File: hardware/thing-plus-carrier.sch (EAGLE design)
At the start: 6 parts, among them J1 THING_PLUS, U1 OKI-78SR-5/1.5-W36H-C

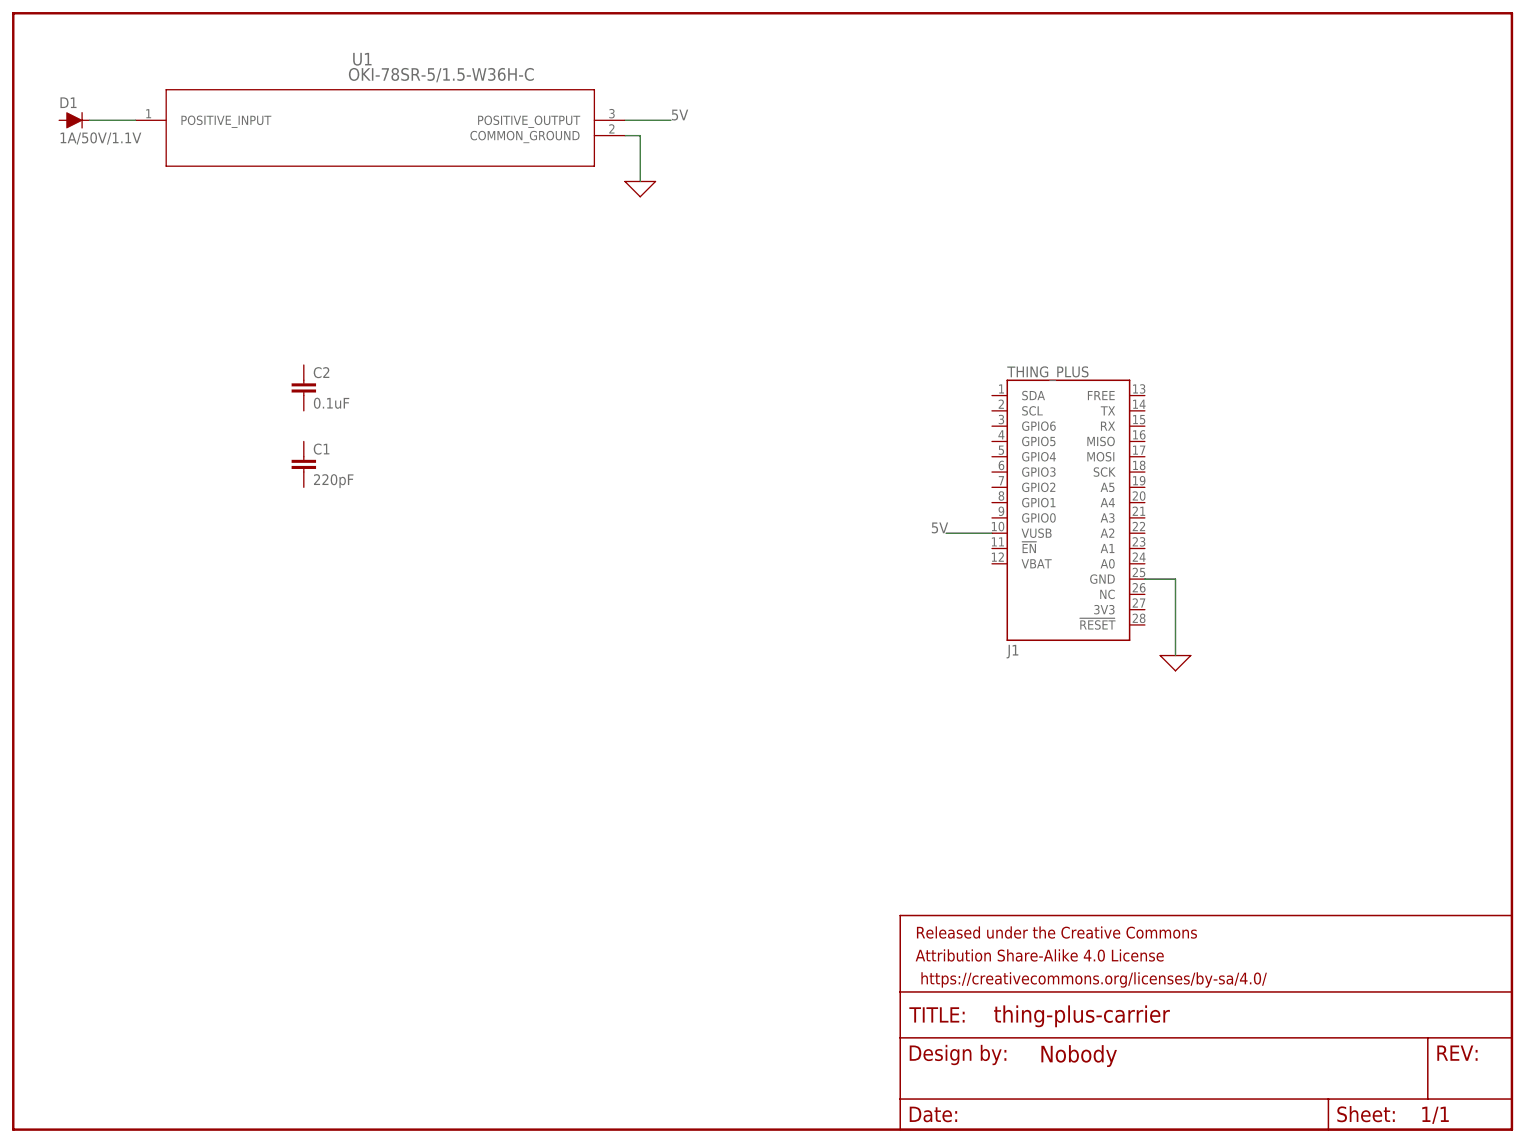
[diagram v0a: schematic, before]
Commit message: laying out featherwing schematic
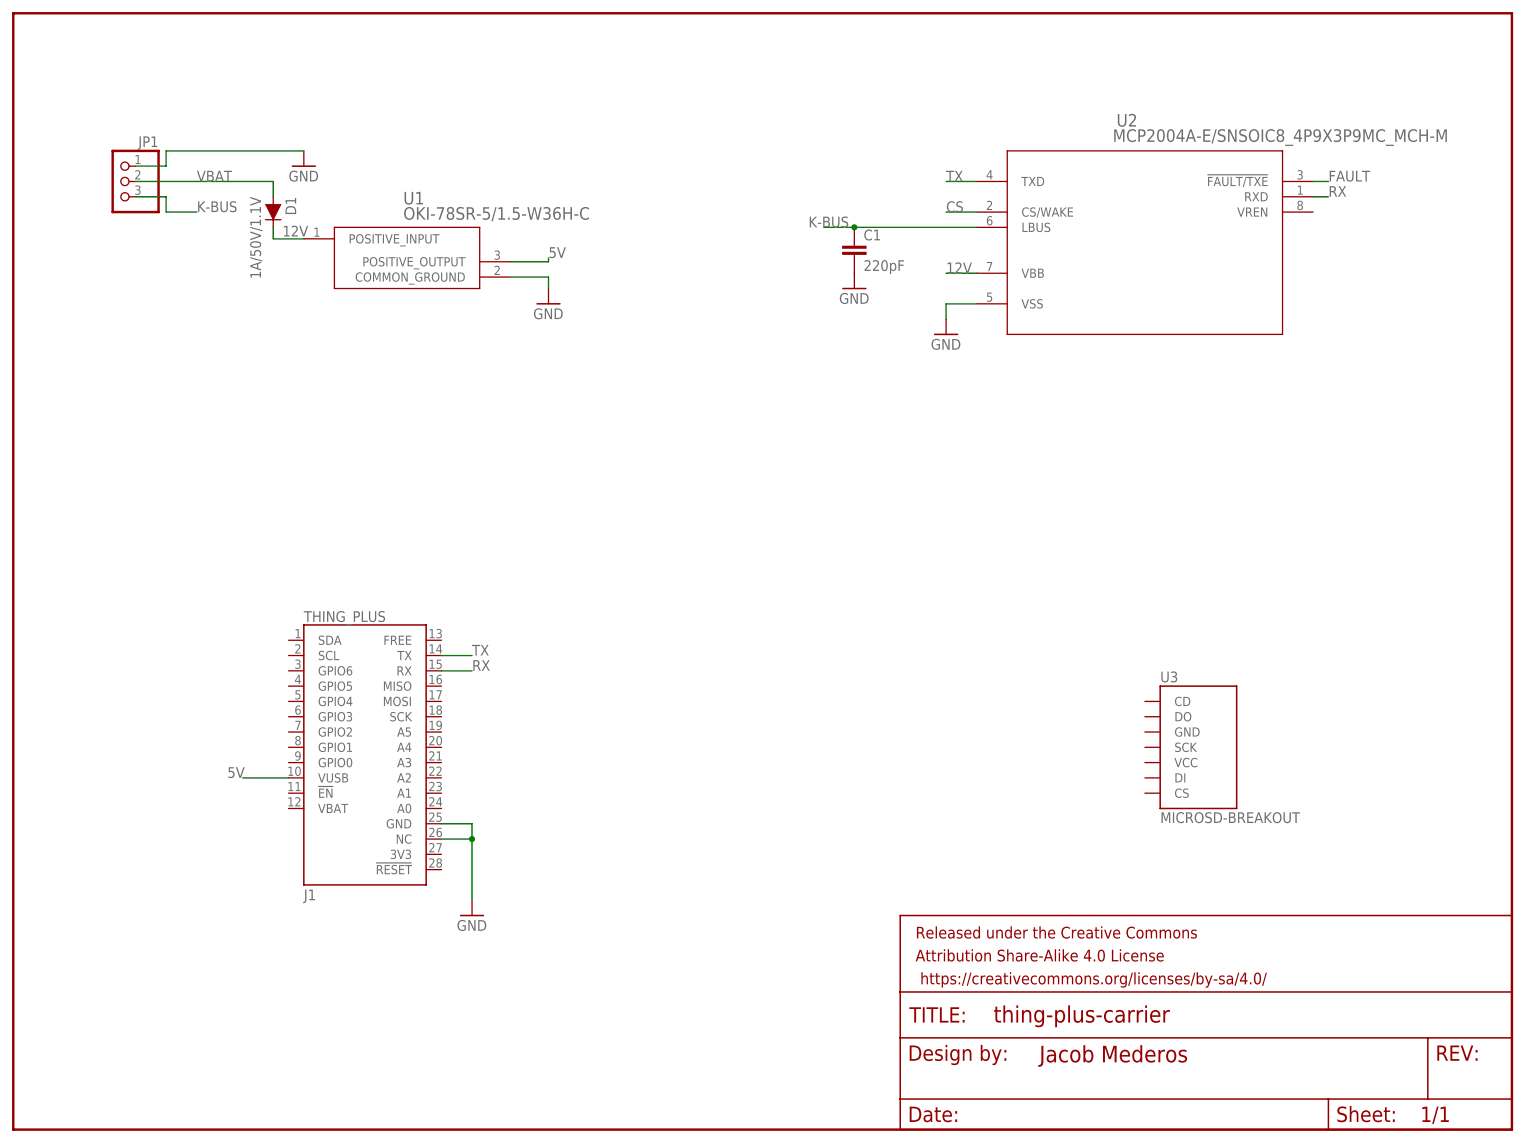
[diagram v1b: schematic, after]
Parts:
- removed C2: 0.1uF, SparkFun-Capacitors:0.1UF-KIT-EZ-50V-20%
- added JP1: (no value), adafruit:PINHD-1X3
- added U2: MCP2004A-E/SNSOIC8_4P9X3P9MC_MCH-M, kbus-feather-carrier-bom:MCP2004A-E/SNSOIC8_4P9X3P9MC_MCH-M
- added U3: MICROSD-BREAKOUT, SparkFun-Boards:MICROSD-BREAKOUT
- FRAME1: DESIGNER (none) -> Jacob Mederos
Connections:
- removed net 0: J1.GND, U1.COMMON_GROUND
- removed net N$1: D1.C, U1.POSITIVE_INPUT
- new net 12V: D1.C, U1.POSITIVE_INPUT, U2.VBB
- new net CS: U2.CS/WAKE
- new net FAULT: U2.!FAULT/TXE
- new net GND: C1.2, J1.GND, J1.NC, JP1.1, U1.COMMON_GROUND, U2.VSS
- new net K-BUS: C1.1, JP1.3, U2.LBUS
- new net RX: J1.RX, U2.RXD
- new net TX: J1.TX, U2.TXD
- new net VBAT: D1.A, JP1.2
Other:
- moved on the sheet: C1, D1, J1, U1

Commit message: Finished rev.1 board []~(￣▽￣)~* ; Updated docs
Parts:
- removed J1: THING_PLUS, SparkFun-Boards:THING_PLUS
- added C2: 22uF, adafruit:C-USC1206K
- added ESP32-THING-PLUS: THING_PLUS, SparkFun-Boards:THING_PLUS
- added LED1, LED2, LED3, LED4: (no value), adafruit:LEDCHIPLED_0805
- added R1, R2, R3, R4: 1k, adafruit:R-US_R0805
- JP1: device adafruit:PINHD-1X3 -> kbus-feather-carrier-bom:PINHD-1X3
- U3: device SparkFun-Boards:MICROSD-BREAKOUT -> kbus-feather-carrier-bom:MICROSD-BREAKOUT
- renumbered U1 to OKI-78SR, U2 to MCP2004A
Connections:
- removed net CS: MCP2004A.CS/WAKE
- new net 3V3: ESP32-THING-PLUS.3V3, U3.VCC
- new net CD: ESP32-THING-PLUS.GPIO5, U3.CD
- new net CIPO: ESP32-THING-PLUS.GPIO1, U3.DO
- new net COPI: ESP32-THING-PLUS.GPIO0, U3.DI
- new net N$1: ESP32-THING-PLUS.A5, R3.1
- new net N$2: ESP32-THING-PLUS.A0, R1.1
- new net N$3: ESP32-THING-PLUS.A3, R2.1
- new net N$4: ESP32-THING-PLUS.MOSI, R4.1
- new net N$5: LED4.A, R4.2
- new net N$6: LED3.A, R3.2
- new net N$7: LED2.A, R2.2
- new net N$8: LED1.A, R1.2
- new net SCK: ESP32-THING-PLUS.GPIO6, U3.SCK
- new net SD-CS: ESP32-THING-PLUS.GPIO4, U3.CS
- new net TRX-CS: ESP32-THING-PLUS.FREE, MCP2004A.CS/WAKE
- net 12V: now also C2.1
- net 5V: now also ESP32-THING-PLUS.VUSB; no longer J1.VUSB
- net FAULT: now also ESP32-THING-PLUS.GPIO2
- net GND: now also C2.2, ESP32-THING-PLUS.GND, ESP32-THING-PLUS.NC, LED1.C, LED2.C, LED3.C, LED4.C, U3.GND; no longer J1.GND, J1.NC
- net RX: now also ESP32-THING-PLUS.RX; no longer J1.RX
- net TX: now also ESP32-THING-PLUS.TX; no longer J1.TX
